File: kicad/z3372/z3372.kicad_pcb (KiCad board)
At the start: 4 copper layers, 80 x 80 mm, 134 parts, among them J1 Conn_01x01, J2 Conn_01x02, J3 Conn_02x20_Odd_Even, Q1 MMBT3904, Q2 MMBT3904, Q3 MMBT3904, Q4 MMBT3904, U1 MUX508, U11 DG442xY, U13 LM4040AIM3-2.5, U15 M24C02-WMN, U18 NE5532, U19 L79L05_TO92, U2 MUX508, U3 TL074, U4 TL074, U5 TL072, U7 CAT9555YI-T2, U8 AS3372, U9 AD5328

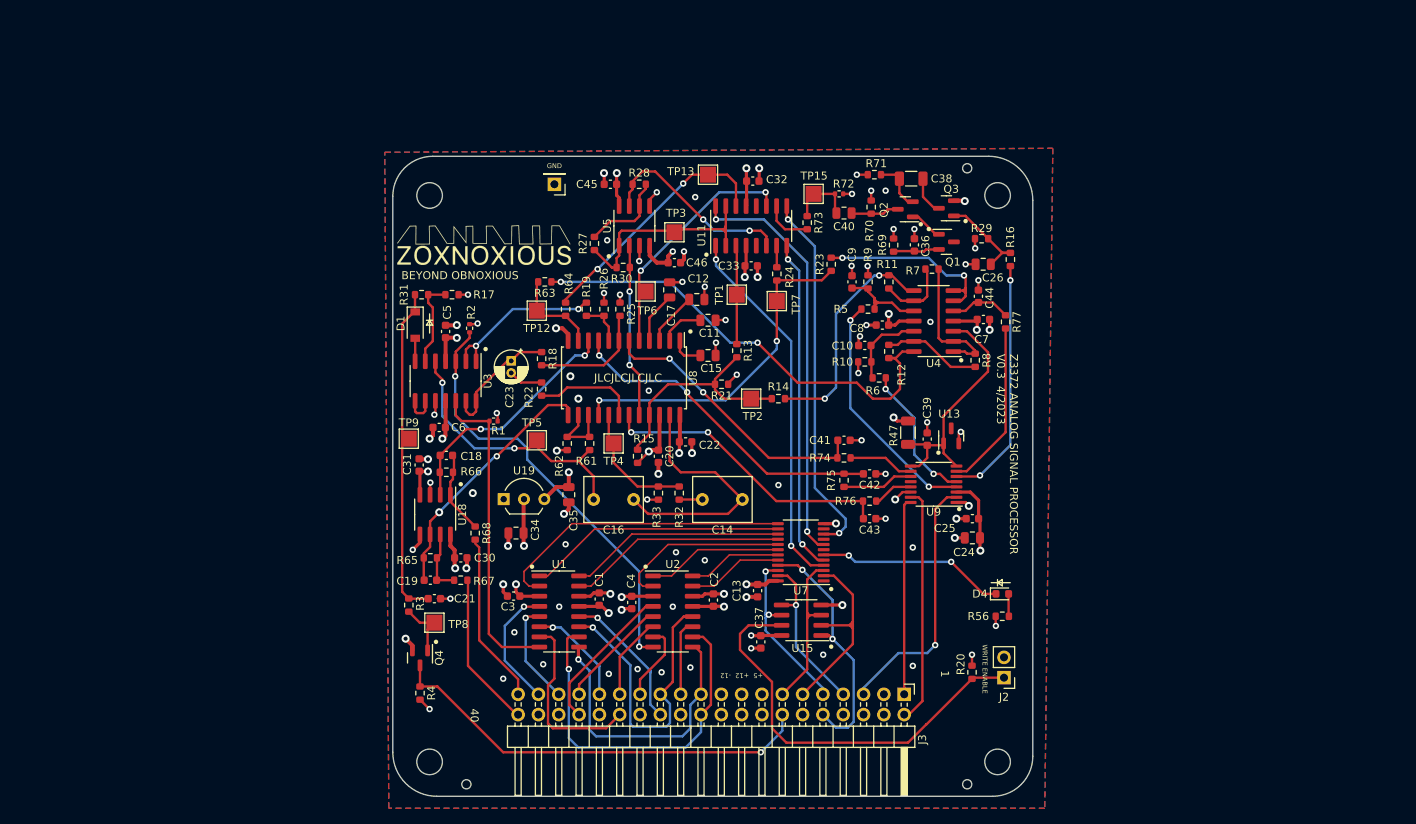
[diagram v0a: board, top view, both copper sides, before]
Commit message: schematic completed, working on place and route
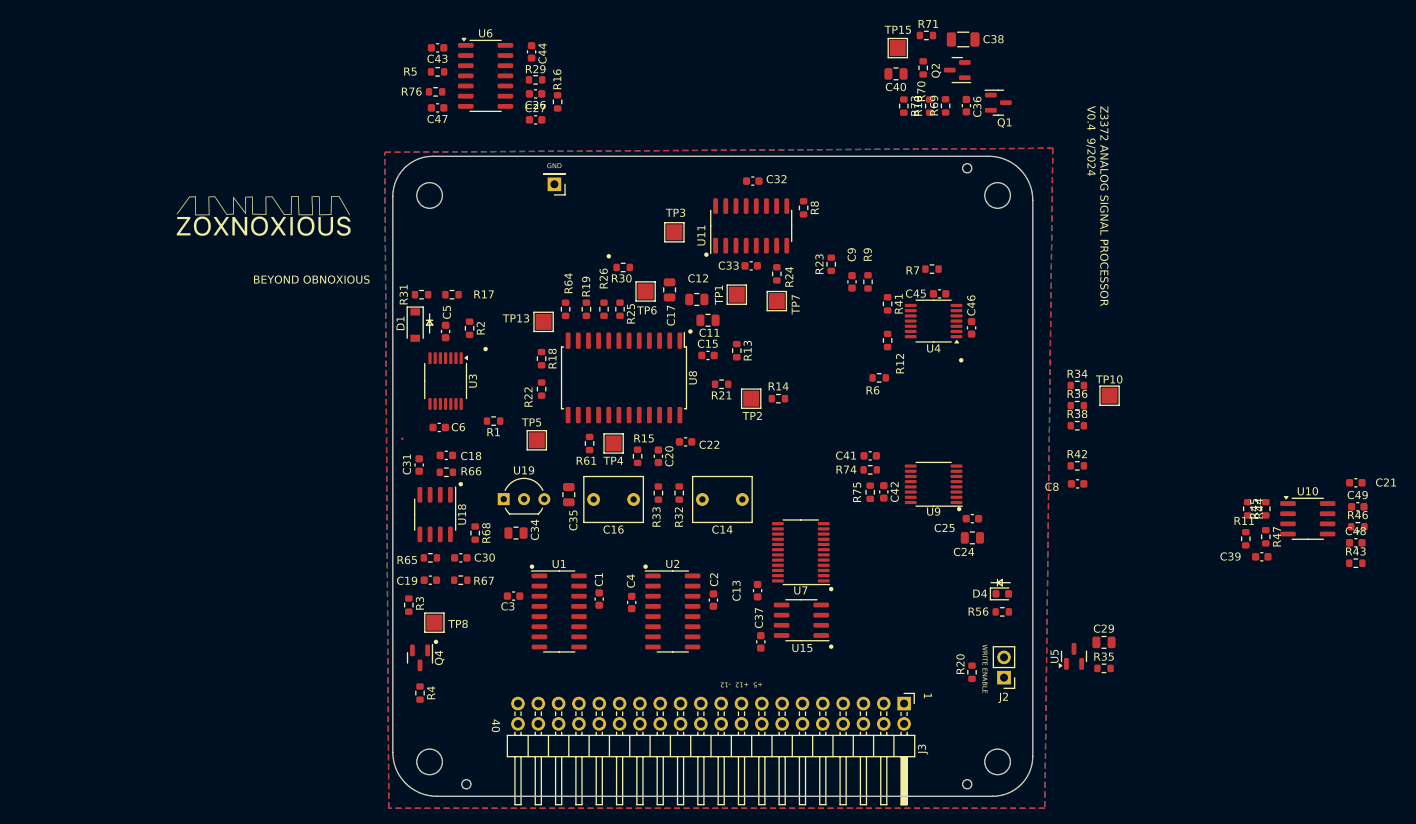
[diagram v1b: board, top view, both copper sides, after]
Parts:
- removed C10: 10n, Capacitor_SMD:C_0603_1608Metric
- removed C23: 2.2u, Capacitor_THT:CP_Radial_D4.0mm_P1.50mm
- removed C7: 0.1u, Capacitor_SMD:C_0603_1608Metric
- removed Q3: MMBT3904, Package_TO_SOT_SMD:SOT-23
- removed R27, R28: 47k, Resistor_SMD:R_0603_1608Metric
- removed R62: 1k, Resistor_SMD:R_0603_1608Metric
- removed R63: 10k, Resistor_SMD:R_0603_1608Metric
- removed R72: 100k, Resistor_SMD:R_0402_1005Metric
- removed R77: 15k, Resistor_SMD:R_0603_1608Metric
- removed TP12, TP9: TestPoint, TestPoint:TestPoint_Pad_2.0x2.0mm
- removed U13: LM4040AIM3-2.5, Package_TO_SOT_SMD:SOT-23
- added C27: 4n7, Capacitor_SMD:C_0603_1608Metric, F.Cu at (83.2, 20.8)
- added C29: 1u, Capacitor_SMD:C_0805_2012Metric, F.Cu at (154.3, 86.1)
- added C47: 0.1u, Capacitor_SMD:C_0603_1608Metric, F.Cu at (71.0, 19.2)
- added C48: 47n, Capacitor_SMD:C_0603_1608Metric, F.Cu at (185.8, 73.6)
- added C49: 22n, Capacitor_SMD:C_0603_1608Metric, F.Cu at (186.0, 69.1)
- added R34: 20k, Resistor_SMD:R_0603_1608Metric, F.Cu at (151.0, 54.0)
- added R35: 4k7, Resistor_SMD:R_0603_1608Metric, F.Cu at (154.3, 89.3)
- added R36: 20k, Resistor_SMD:R_0603_1608Metric, F.Cu at (151.0, 56.5)
- added R38: 510, Resistor_SMD:R_0603_1608Metric, F.Cu at (151.0, 59.0)
- added R41: 20k, Resistor_SMD:R_0603_1608Metric, F.Cu at (127.2, 43.8)
- added R42: 2k, Resistor_SMD:R_0603_1608Metric, F.Cu at (151.0, 64.0)
- added R43: 20k, Resistor_SMD:R_0603_1608Metric, F.Cu at (185.8, 76.2)
- added R44: 20k, Resistor_SMD:R_0603_1608Metric, F.Cu at (172.3, 69.4)
- added R45: 20k, Resistor_SMD:R_0603_1608Metric, F.Cu at (174.5, 69.4)
- added R46: 20k, Resistor_SMD:R_0603_1608Metric, F.Cu at (186.0, 71.6)
- added TP10: TestPoint, TestPoint:TestPoint_Pad_2.0x2.0mm, F.Cu at (155.0, 55.2)
- added U10: TL072, Package_SO:SOIC-8_3.9x4.9mm_P1.27mm, F.Cu at (179.8, 70.6)
- added U6: AS3360-Audio, Package_SO:SOIC-14_3.9x8.7mm_P1.27mm, F.Cu at (77.0, 15.2)
- C14, C16: value 2.2u -> 2u2
- C15: footprint Capacitor_SMD:C_0805_2012Metric -> Capacitor_SMD:C_0603_1608Metric
- C24, C40: value 4.7u -> 4u7
- C26: value 22n -> 0.1u; footprint Capacitor_SMD:C_0805_2012Metric -> Capacitor_SMD:C_0603_1608Metric
- C43, C44: value 10n -> 0.1u
- C9: value 68n -> 33n
- R1, R2: footprint Resistor_SMD:R_0402_1005Metric -> Resistor_SMD:R_0603_1608Metric
- R10: value 20k -> 330k
- R11: value 3k3 -> 20k
- R13: value 82k -> 36k
- R14: value 20k -> 18k
- R16: value 18k -> 15k
- R22: value 22k -> 20k
- R23: value 10k -> 20k
- R24: value 24k -> 30k
- R3: value 4k7 -> 100k
- R47: value 4k7 -> 20k; footprint Resistor_SMD:R_1206_3216Metric -> Resistor_SMD:R_0603_1608Metric
- R5: value 2k4 -> 9k1
- R64, R8: value 20k -> 30k
- R67, R68: value 1k -> 51
- R69: value 680k -> 330k
- R7: value 8k2 -> 15k
- R73: value 2k -> 36k
- R9: value 120k -> 12k
- U3, U4: footprint Package_SO:SOIC-14_3.9x8.7mm_P1.27mm -> Package_SO:TSSOP-14_4.4x5mm_P0.65mm
- U5: value TL072 -> LM4040AIM3-2.5; footprint Package_SO:SOIC-8_3.9x4.9mm_P1.27mm -> Package_TO_SOT_SMD:SOT-23
- moved C21 116.1 mm to (185.8, 66.1)
- moved C43 79.9 mm to (71.0, 11.8)
- moved U5 76.9 mm to (150.6, 87.8)
- moved R76 74.6 mm to (70.8, 17.2)
- moved C44 63.7 mm to (82.8, 12.2)
- moved R5 61.4 mm to (71.0, 14.8)
- moved R16 59.9 mm to (86.0, 18.5)
- moved C26 59.9 mm to (83.2, 17.5)
- moved R29 59.2 mm to (83.2, 15.8)
- moved R11 55.0 mm to (172.0, 73.1)
- moved R47 46.6 mm to (174.5, 72.9)
- moved C39 44.3 mm to (174.0, 75.4), turned to 180 degrees
- moved C45 43.4 mm to (133.8, 42.5)
- moved C46 38.0 mm to (137.8, 46.8), turned to 90 degrees
- moved R10 33.0 mm to (132.5, 19.0), turned to 90 degrees
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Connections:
- net /DAC/MOD_AMOUNT_VCA3_DAC renamed /DAC/MOD_AMOUNT_DAC
- C21 pad 1: Net-(C21-Pad1) -> +12V
- C38 pad 2: Net-(C38-Pad2) -> GND
- C39 pad 1: /DAC/VREF_2.5V -> -12V
- C43 pad 1: /DAC/MOD_AMOUNT_VCA3_CV -> /DAC/MOD_AMOUNT_CV
- C44 pad 1: Net-(C44-Pad1) -> GND
- C44 pad 2: GND -> +12V
- C8 pad 1: GND -> Net-(C8-Pad1)
- C8 pad 2: -12V -> GND
- C9 pad 1: Net-(C9-Pad1) -> Net-(U3C--)
- C9 pad 2: GND -> /DAC/RESONANCE_CV
- D1 pad 1: Net-(C21-Pad1) -> Net-(D1-K)
- R10 pad 1: GND -> +12V
- R10 pad 2: Net-(C10-Pad1) -> Net-(R10-Pad2)
- R11 pad 1: Net-(R11-Pad1) -> /DAC/PAN_VCA_DAC
- R11 pad 2: /DAC/VCF_CV -> Net-(U10A-+)
- R12 pad 1: Net-(R12-Pad1) -> Net-(U4D--)
- R12 pad 2: /DAC/PAN_VCA_CV -> /filter_as3372/PAN_CV
- R14 pad 2: /DAC/VCF_CV -> Net-(C8-Pad1)
- R22 pad 1: Net-(R22-Pad1) -> Net-(U6A-Signal)
- R22 pad 2: Net-(C23-Pad2) -> /VCF_SIGNAL1
- R23 pad 1: Net-(R23-Pad1) -> Net-(U4A--)
- R24 pad 1: Net-(R23-Pad1) -> Net-(U4A--)
- R3 pad 1: Net-(C21-Pad1) -> Net-(D1-K)
- R30 pad 1: Net-(R30-Pad1) -> Net-(U4B--)
- R31 pad 1: Net-(C21-Pad1) -> Net-(D1-K)
- R47 pad 1: +5V -> Net-(U10B--)
- R47 pad 2: /DAC/VREF_2.5V -> /DAC/FINAL_VCA4_CV
- R5 pad 1: /DAC/VCF_CV_DAC -> GND
- R5 pad 2: Net-(C9-Pad1) -> /DAC/MOD_AMOUNT_CV
- R6 pad 1: /DAC/PAN_VCA_CV_DAC -> /DAC/PAN_VCA_CV
- R6 pad 2: Net-(C10-Pad1) -> Net-(U4D--)
- R61 pad 2: Net-(R61-Pad2) -> Net-(U8C-VCA4_IN)
- R64 pad 1: Net-(R63-Pad1) -> Net-(U4C--)
- R64 pad 2: /filter_as3372/VCA_FM -> /filter_as3372/VCA4_FM
- R69 pad 1: +12V -> Net-(R10-Pad2)
- R7 pad 1: /DAC/VREF_2.5V_BUFFERED -> /DAC/RESONANCE_DAC
- R7 pad 2: Net-(R11-Pad1) -> Net-(U3C--)
- R73 pad 2: /filter_as3372/WHITE_NOISE -> Net-(U6B-Signal)
- R76 pad 2: /DAC/MOD_AMOUNT_VCA3_CV -> /DAC/MOD_AMOUNT_CV
- R8 pad 1: /DAC/VREF_2.5V_BUFFERED -> Net-(U4D--)
- R8 pad 2: Net-(R12-Pad1) -> /filter_as3372/PAN_FM
- R9 pad 1: GND -> Net-(U3C--)
- R9 pad 2: Net-(C9-Pad1) -> /DAC/RESONANCE_CV
- TP1 pad 1: /filter_as3372/VCF_FM -> /filter_as3372/PAN_CV
- TP13 pad 1: /filter_as3372/VCA_FM -> Net-(U8C-VCA4_CV)
- TP6 pad 1: Net-(TP6-Pad1) -> /filter_as3372/WHITE_NOISE
- TP7 pad 1: Net-(R23-Pad1) -> Net-(U8B-Res_CV)
- U11 pad 10: /filter_as3372/WHITE_NOISE -> /filter_as3372/PAN_FM
- U11 pad 11: Net-(TP6-Pad1) -> /filter_as3372/MOD_VCA_OUT
- U11 pad 14: /filter_as3372/VCA_FM -> /filter_as3372/VCA4_FM
- U11 pad 6: Net-(R28-Pad1) -> /filter_as3372/MOD_VCA_OUT
- U11 pad 9: /WHITE_NOISE_CTRL -> /PAN_FM_CTRL
- U3 pad 8: Net-(U3-Pad8) -> /DAC/RESONANCE_CV
- U3 pad 9: Net-(U3-Pad8) -> Net-(U3C--)
- U4 pad 1: /DAC/VREF_2.5V_BUFFERED -> Net-(U8B-Res_CV)
- U4 pad 10: Net-(C9-Pad1) -> GND
- U4 pad 12: Net-(C10-Pad1) -> GND
- U4 pad 13: Net-(R12-Pad1) -> Net-(U4D--)
- U4 pad 14: /DAC/PAN_VCA_CV -> /filter_as3372/PAN_CV
- U4 pad 2: /DAC/VREF_2.5V_BUFFERED -> Net-(U4A--)
- U4 pad 3: /DAC/VREF_2.5V -> GND
- U4 pad 5: Net-(C44-Pad1) -> GND
- U4 pad 6: /DAC/RESONANCE_CV -> Net-(U4B--)
- U4 pad 7: /DAC/RESONANCE_CV -> /filter_as3372/MOD_VCA_OUT
- U4 pad 8: /DAC/VCF_CV -> Net-(U8C-VCA4_CV)
- U4 pad 9: Net-(R11-Pad1) -> Net-(U4C--)
- U5 pad 1: /filter_as3372/MOD_VCA_OUT -> /VREF_2.5V
- U5 pad 2: Net-(R30-Pad1) -> GND
- U5 pad 3: GND -> (no net)
- U7 pad 10: /WHITE_NOISE_CTRL -> unconnected-(U7-IO0_6-Pad10)
- U7 pad 9: unconnected-(U7-Pad9) -> /PAN_FM_CTRL
- U8 pad 11: Net-(R63-Pad1) -> /filter_as3372/PAN_CV
- U8 pad 14: Net-(R61-Pad2) -> Net-(U8C-VCA4_OUT)
- U8 pad 15: Net-(R61-Pad2) -> Net-(U8C-VCA4_OUT)
- U8 pad 16: Net-(R23-Pad1) -> Net-(U8B-Res_CV)
- U8 pad 18: Net-(R22-Pad1) -> Net-(U8C-VCA4_IN)
- U8 pad 19: /DAC/MOD_AMOUNT_VCA3_CV -> Net-(U8C-VCA4_CV)
- U8 pad 20: Net-(R30-Pad1) -> Net-(U8C-VCA4_OUT)
- U8 pad 5: Net-(TP6-Pad1) -> /filter_as3372/WHITE_NOISE
- U9 pad 12: unconnected-(U9-Pad12) -> /DAC/VCA4_DAC
- U9 pad 4: /DAC/VCF_CV_DAC -> /DAC/VCF_CV
- U9 pad 5: /DAC/PAN_VCA_CV_DAC -> /DAC/PAN_VCA_DAC
- U9 pad 8: /DAC/VREF_2.5V -> /VREF_2.5V
- U9 pad 9: /DAC/VREF_2.5V -> /VREF_2.5V
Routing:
- net GND: track 197.0 -> 100.1 mm, vias 86 -> 0
- net +12V: track 94.9 -> 0.00 mm, vias 10 -> 0
- net +5V: track 75.4 -> 0.00 mm, vias 7 -> 0
- net /DAC/PAN_VCA_CV: track 58.5 -> 0.00 mm, vias 2 -> 0
- net /GPIO_MODULE_DRIVEN: track 54.5 -> 0.00 mm, vias 1 -> 0
- net Net-(U2-D): track 54.2 -> 0.00 mm, vias 2 -> 0
- net Net-(J2-Pin_1): track 52.2 -> 0.00 mm
- net /VCA_FM_CTRL: track 51.8 -> 0.00 mm, vias 2 -> 0
- net /VCF_FM_CTRL: track 46.5 -> 0.00 mm, vias 2 -> 0
- net /WHITE_NOISE_CTRL: track 46.2 -> 0.00 mm, vias 2 -> 0
- net /CARD1_OUT2: track 46.0 -> 0.00 mm, vias 1 -> 0
- net Net-(R23-Pad1): track 42.6 -> 0.00 mm, vias 2 -> 0
- net Net-(C21-Pad1): track 42.4 -> 0.00 mm
- net /RES_FM_CTRL: track 41.6 -> 0.00 mm, vias 2 -> 0
- net /DAC/SIG2_VCA2_CV: track 41.2 -> 0.00 mm, vias 2 -> 0
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- removed copper zone on In2.Cu, net +12V
- removed copper zone on In2.Cu, net +5V
- removed copper zone on In2.Cu, net -12V
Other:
- board text added: "Z3372 ANALOG SIGNAL PROCESSOR V0.4 9/2024"
- board text removed: "JLCJLCJLCJLC"
- board text removed: "Z3372 ANALOG SIGNAL PROCESSOR V0.3 4/2023"

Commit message: placement improvements
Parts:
- removed U10: TL072, Package_SO:SOIC-8_3.9x4.9mm_P1.27mm
- added U12: TL074, Package_SO:TSSOP-14_4.4x5mm_P0.65mm, F.Cu at (138.0, 44.2)
- moved C38 76.0 mm to (69.9, 47.0), turned to 180 degrees
- moved J1 74.6 mm to (160.0, 34.8)
- moved Q1 74.2 mm to (69.6, 38.5), turned to 180 degrees
- moved Q2 72.3 mm to (69.6, 43.2), turned to 0 degrees
- moved R71 67.7 mm to (75.2, 47.0), turned to -90 degrees
- moved C36 66.9 mm to (73.0, 38.2), turned to -90 degrees
- moved R70 65.4 mm to (73.0, 43.0), turned to 90 degrees
- moved R69 62.3 mm to (75.2, 38.2), turned to 90 degrees
- moved TP10 62.0 mm to (93.2, 61.2)
- moved R38 60.8 mm to (90.2, 61.2), turned to -90 degrees
- moved C40 59.8 mm to (75.5, 43.0), turned to 90 degrees
- moved R73 58.8 mm to (77.5, 47.0)
- moved R10 58.3 mm to (77.5, 38.2), turned to -90 degrees
- moved TP15 58.3 mm to (79.5, 43.2), turned to 90 degrees
- moved C21 55.3 mm to (138.1, 38.0), turned to 90 degrees
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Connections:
- C9 pad 1: Net-(U3C--) -> Net-(U12B--)
- R17 pad 1: Net-(U3B--) -> Net-(U3A--)
- R22 pad 1: Net-(U6A-Signal) -> Net-(U6B-Signal)
- R31 pad 2: Net-(U3B--) -> Net-(U3A--)
- R7 pad 2: Net-(U3C--) -> Net-(U12B--)
- R73 pad 2: Net-(U6B-Signal) -> Net-(U6A-Signal)
- R9 pad 1: Net-(U3C--) -> Net-(U12B--)
- U11 pad 14: /filter_as3372/VCA4_FM -> /filter_as3372/RES_FM
- U11 pad 16: /VCA_FM_CTRL -> /RES_FM_CTRL
- U11 pad 7: /filter_as3372/RES_FM -> /filter_as3372/VCA4_FM
- U11 pad 8: /RES_FM_CTRL -> /VCA_FM_CTRL
- U3 pad 1: /VCF_SIGNAL2 -> Net-(D1-A)
- U3 pad 10: GND -> Net-(U2-D)
- U3 pad 2: /VCF_SIGNAL2 -> Net-(U3A--)
- U3 pad 3: Net-(U2-D) -> /VCF_RAW
- U3 pad 5: /VCF_RAW -> GND
- U3 pad 7: Net-(D1-A) -> Net-(U3B--)
- U3 pad 8: /DAC/RESONANCE_CV -> /VCF_SIGNAL2
- U3 pad 9: Net-(U3C--) -> /VCF_SIGNAL2
- U6 pad 10: /DAC/NOISE_CONTROL_CV -> /DAC/MOD_AMOUNT_CV
- U6 pad 13: /filter_as3372/WHITE_NOISE -> Net-(U4B--)
- U6 pad 2: Net-(U4B--) -> /filter_as3372/WHITE_NOISE
- U6 pad 5: /DAC/MOD_AMOUNT_CV -> /DAC/NOISE_CONTROL_CV

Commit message: time to start routing?
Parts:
- moved J1 126.2 mm to (34.0, 42.8), turned to -90 degrees
- moved U19 51.3 mm to (125.9, 67.0), turned to 90 degrees
- moved C34 44.5 mm to (121.5, 65.5), turned to 90 degrees
- moved C35 38.1 mm to (121.5, 61.2), turned to -90 degrees
- moved TP1 36.1 mm to (91.5, 44.2)
- moved C18 20.2 mm to (72.2, 56.6), turned to 0 degrees
- moved C31 19.0 mm to (68.8, 57.8), turned to 90 degrees
- moved R68 17.9 mm to (75.2, 59.5), turned to -90 degrees
- moved TP8 17.7 mm to (75.5, 75.2), turned to 180 degrees
- moved R3 16.3 mm to (78.2, 74.5), turned to -90 degrees
- moved R66 16.0 mm to (72.2, 58.7), turned to 0 degrees
- moved Q4 13.3 mm to (74.5, 79.5), turned to -90 degrees
- moved R67 12.3 mm to (70.2, 73.5)
- moved R4 11.2 mm to (73.5, 83.0), turned to 180 degrees
- moved C19 11.0 mm to (70.2, 71.5), turned to 0 degrees
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
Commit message: figuring out power routing
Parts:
- moved C13 1.16 mm to (112.1, 81.0)
- moved C37 1.14 mm to (112.5, 87.6)
- moved U15 1.14 mm to (117.6, 84.9)
- moved U7 1.14 mm to (117.5, 76.4)
- moved C47 0.55 mm to (83.0, 37.5)
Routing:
- net +5V: track 0.00 -> 145.1 mm, vias 0 -> 5
- net -12V: track 0.00 -> 114.3 mm, vias 0 -> 5
- net +12V: track 0.00 -> 16.1 mm

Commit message: checkpoint z3372
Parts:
- moved R2 30.8 mm to (86.2, 58.0), turned to -90 degrees
- moved TP5 9.52 mm to (100.2, 61.2)
- moved R32 8.75 mm to (93.8, 71.0)
- moved R33 8.75 mm to (93.8, 69.0)
- moved TP4 8.75 mm to (93.8, 65.2)
- moved R71 5.30 mm to (70.8, 47.5), turned to 180 degrees
- moved C16 2.00 mm to (99.2, 70.8)
- moved R4 1.80 mm to (75.2, 83.0), turned to 0 degrees
- moved C4 1.50 mm to (95.2, 79.5), turned to -90 degrees
- moved C14 1.50 mm to (106.2, 65.8)
- moved C2 1.50 mm to (105.5, 82.5), turned to 90 degrees
- moved C3 1.50 mm to (81.0, 79.5), turned to -90 degrees
- moved R61 1.35 mm to (97.5, 61.0)
- moved C21 0.94 mm to (138.5, 38.5), turned to 0 degrees
- moved C6 0.90 mm to (84.2, 58.0), turned to -90 degrees
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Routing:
- net +12V: track 16.1 -> 224.7 mm, vias 0 -> 12
- net -12V: track 114.3 -> 229.3 mm, vias 5 -> 9
- net /GPIO_MODULE_DRIVEN: track 0.00 -> 57.8 mm
- net /CARD1_OUT2: track 0.00 -> 44.9 mm, vias 0 -> 1
- net /VCF_SIG1_EN: track 0.00 -> 37.4 mm
- net /CARD1_OUT1: track 0.00 -> 35.3 mm, vias 0 -> 1
- net /VCF_SIG1_CTRL0: track 0.00 -> 32.7 mm
- net /CARD2_OUT2: track 0.00 -> 29.3 mm, vias 0 -> 1
- net /VCF_SIG1_CTRL2: track 0.00 -> 27.7 mm
- net /VCF_SIG1_CTRL1: track 0.00 -> 27.5 mm
- net /CARD4_OUT2: track 0.00 -> 23.2 mm
- net /VCF_SIG2_EN: track 0.00 -> 22.2 mm
- net /CARD6_OUT1: track 0.00 -> 20.1 mm
- net /CARD3_OUT1: track 0.00 -> 18.7 mm, vias 0 -> 1
- net /VCF_SIG2_CTRL0: track 0.00 -> 17.4 mm
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
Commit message: continue routing
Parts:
- moved C41 0.75 mm to (125.0, 72.8)
- moved C42 0.75 mm to (125.0, 76.3)
- moved R74 0.75 mm to (127.8, 73.5)
- moved R75 0.75 mm to (127.8, 75.5)
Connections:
- U7 pad 4: /VCF_FM_CTRL -> /LED_CTRL
- U7 pad 5: /RES_FM_CTRL -> unconnected-(U7-IO0_1-Pad5)
- U7 pad 6: /LED_CTRL -> /VCF_FM_CTRL
- U7 pad 7: unconnected-(U7-IO0_3-Pad7) -> /RES_FM_CTRL
- U9 pad 10: /DAC/SIG1_VCA_DAC -> /DAC/VCF_CV
- U9 pad 11: /DAC/SIG2_VCA_DAC -> /DAC/SIG1_VCA_DAC
- U9 pad 12: /DAC/VCA4_DAC -> /DAC/SIG2_VCA_DAC
- U9 pad 4: /DAC/VCF_CV -> /DAC/NOISE_CONTROL_DAC
- U9 pad 6: /DAC/NOISE_CONTROL_DAC -> /DAC/RESONANCE_DAC
- U9 pad 7: /DAC/RESONANCE_DAC -> /DAC/VCA4_DAC
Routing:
- net /DAC/NOISE_CONTROL_DAC: track 0.00 -> 77.3 mm, vias 0 -> 2
- net /DAC/MOD_AMOUNT_DAC: track 0.00 -> 72.6 mm, vias 0 -> 2
- net Net-(J2-Pin_1): track 0.00 -> 50.2 mm, vias 0 -> 1
- net /DAC/RESONANCE_DAC: track 0.00 -> 38.5 mm, vias 0 -> 2
- net /I2C_ADDR0: track 0.00 -> 37.6 mm, vias 0 -> 2
- net /VREF_2.5V: track 0.00 -> 34.3 mm
- net /I2C_ADDR2: track 0.00 -> 29.5 mm, vias 0 -> 1
- net /RES_FM_CTRL: track 0.00 -> 28.9 mm, vias 0 -> 2
- net /filter_as3372/MOD_VCA_OUT: track 0.00 -> 28.7 mm
- net /PAN_FM_CTRL: track 0.00 -> 28.5 mm, vias 0 -> 2
- net /VCF_FM_CTRL: track 0.00 -> 25.6 mm, vias 0 -> 2
- net /VCA_FM_CTRL: track 0.00 -> 25.3 mm, vias 0 -> 2
- net /SPI_CS0: track 0.00 -> 25.1 mm, vias 0 -> 1
- net /DAC/VCA4_DAC: track 0.00 -> 24.4 mm, vias 0 -> 2
- net /I2C_ADDR1: track 0.00 -> 22.3 mm, vias 0 -> 1
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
